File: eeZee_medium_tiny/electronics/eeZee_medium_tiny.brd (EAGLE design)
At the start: 28.7 x 16.3 mm, 11 parts, among them IC1 TINY24/44/84, J2 avrisp, Q1 16MHz

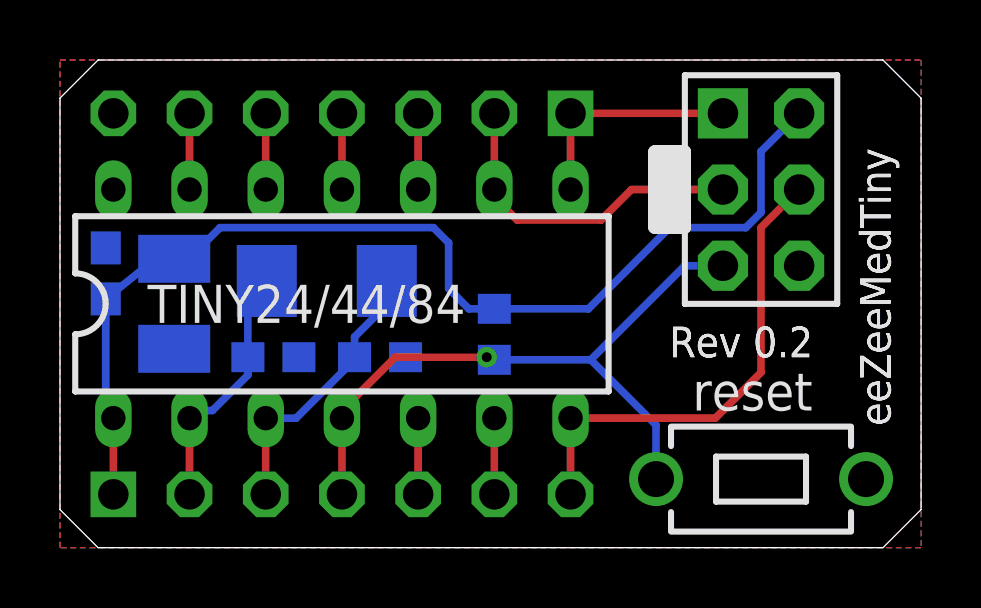
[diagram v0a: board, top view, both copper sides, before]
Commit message: Revised pads for IC, revised 10uF filtering cap footprint to 1206.
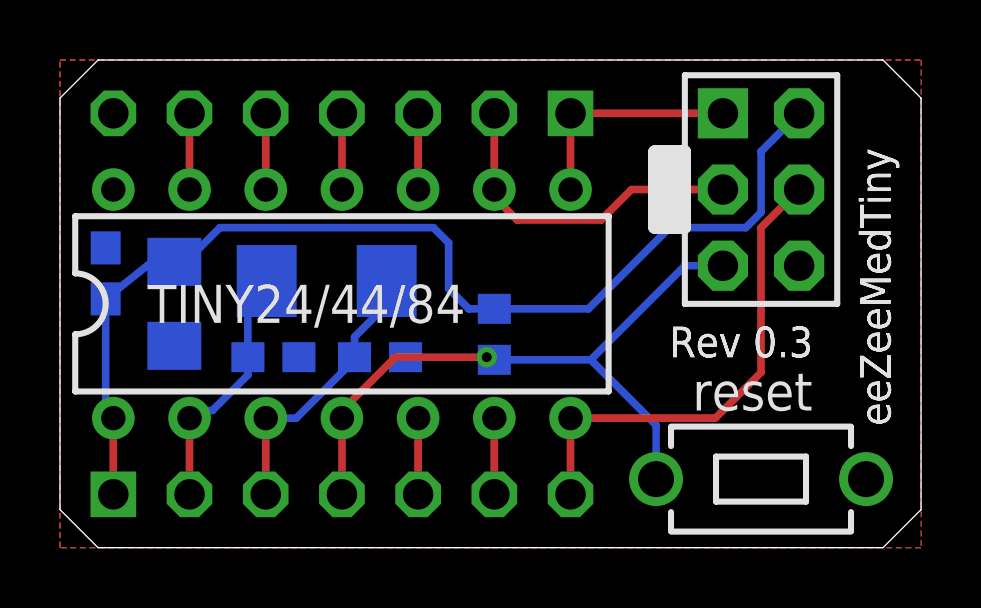
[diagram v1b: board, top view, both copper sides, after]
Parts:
- C2: device mes_rcl:SMC_B -> rcl:C1206
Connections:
- net GND: now also C2.2; no longer C2.-
- net VCC: now also C2.1; no longer C2.+
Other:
- board text added: "Rev 0.3"
- board text removed: "Rev 0.2"
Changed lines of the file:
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@@
 <layer number="19" name="Unrouted" color="6" fill="1" visible="yes" active="yes"/>
 <layer number="20" name="Dimension" color="15" fill="1" visible="yes" active="yes"/>
-<layer number="21" name="tPlace" color="7" fill="1" visible="no" active="yes"/>
-<layer number="22" name="bPlace" color="7" fill="1" visible="no" active="yes"/>
-<layer number="23" name="tOrigins" color="15" fill="1" visible="no" active="yes"/>
-<layer number="24" name="bOrigins" color="15" fill="1" visible="no" active="yes"/>
-<layer number="25" name="tNames" color="7" fill="1" visible="no" active="yes"/>
-<layer number="26" name="bNames" color="7" fill="1" visible="no" active="yes"/>
-<layer number="27" name="tValues" color="7" fill="1" visible="no" active="yes"/>
-<layer number="28" name="bValues" color="7" fill="1" visible="no" active="yes"/>
+<layer number="21" name="tPlace" color="7" fill="1" visible="yes" active="yes"/>
+<layer number="22" name="bPlace" color="7" fill="1" visible="yes" active="yes"/>
+<layer number="23" name="tOrigins" color="15" fill="1" visible="yes" active="yes"/>
+<layer number="24" name="bOrigins" color="15" fill="1" visible="yes" active="yes"/>
+<layer number="25" name="tNames" color="7" fill="1" visible="yes" active="yes"/>
+<layer number="26" name="bNames" color="7" fill="1" visible="yes" active="yes"/>
+<layer number="27" name="tValues" color="7" fill="1" visible="yes" active="yes"/>
+<layer number="28" name="bValues" color="7" fill="1" visible="yes" active="yes"/>
 <layer number="29" name="tStop" color="7" fill="3" visible="yes" active="yes"/>
 <layer number="30" name="bStop" color="7" fill="6" visible="yes" active="yes"/>
@@
 <vertex x="17.5521875" y="7.832015625"/>
 </polygon>
-<text x="20.32" y="6.35" size="1.016" layer="25" font="vector">Rev 0.2</text>
+<text x="20.32" y="6.35" size="1.016" layer="25" font="vector">Rev 0.3</text>
 <text x="27.686" y="4.064" size="1.016" layer="25" font="vector" rot="R90">eeZeeMedTiny</text>
 <wire x1="24.814809375" y1="2.363190625" x2="21.921190625" y2="2.363190625" width="0.2032" layer="22"/>
@@
 <vertex x="17.5521875" y="7.8320125"/>
 </polygon>
-<text x="20.32" y="6.35" size="1.016" layer="121" font="vector" ratio="20">Rev 0.2</text>
+<text x="20.32" y="6.35" size="1.016" layer="121" font="vector" ratio="20">Rev 0.3</text>
 <text x="27.686" y="4.064" size="1.016" layer="121" font="vector" ratio="20" rot="R90">eeZeeMedTiny</text>
 <text x="26.924" y="4.064" size="0.8128" layer="122" font="vector" ratio="25" rot="MR90">bot-thoughts.com</text>
@@
 </element>
 <element name="J2" library="ads4" package="CON6P2R" value="avrisp" x="23.368" y="11.938" smashed="yes" rot="R270"/>
-<element name="C2" library="mes_rcl" package="SMC_B" value="100uF" x="3.81" y="8.128" smashed="yes" rot="MR270">
+<element name="C2" library="rcl" package="C1206" value="100uF" x="3.81" y="8.128" smashed="yes" rot="MR270">
 <attribute name="PARTNO" value="MCTT21X106M6R3CT" x="3.81" y="8.128" size="1.27" layer="28" font="vector" ratio="16" rot="MR270" display="off"/>
 <attribute name="BOM" value="EXCLUDE" x="3.81" y="8.128" size="1.27" layer="28" font="vector" ratio="16" rot="MR270" display="off"/>
@@
 <vertex x="0" y="0"/>
 </polygon>
-<contactref element="C2" pad="-"/>
+<contactref element="C2" pad="2"/>
 <contactref element="C4" pad="2"/>
 <contactref element="C5" pad="2"/>
@@
 <contactref element="J2" pad="2"/>
 <contactref element="J2" pad="2"/>
-<contactref element="C2" pad="+"/>
+<contactref element="C2" pad="1"/>
 <contactref element="JP4" pad="1"/>
 <contactref element="IC1" pad="1"/>
 <contactref element="IC1" pad="1"/>
 <wire x1="1.778" y1="1.778" x2="1.778" y2="4.318" width="0.254" layer="1"/>
-<wire x1="3.81" y1="9.628" x2="3.19" y2="9.628" width="0.254" layer="16"/>
+<wire x1="3.81" y1="9.528" x2="3.19" y2="9.628" width="0.254" layer="16"/>
 <wire x1="3.19" y1="9.628" x2="1.524" y2="8.294" width="0.254" layer="16"/>
-<wire x1="3.81" y1="9.628" x2="4.294" y2="9.628" width="0.254" layer="16"/>
+<wire x1="3.81" y1="9.528" x2="4.294" y2="9.628" width="0.254" layer="16"/>
 <wire x1="4.294" y1="9.628" x2="5.334" y2="10.668" width="0.254" layer="16"/>
 <wire x1="5.334" y1="10.668" x2="12.446" y2="10.668" width="0.254" layer="16"/>
